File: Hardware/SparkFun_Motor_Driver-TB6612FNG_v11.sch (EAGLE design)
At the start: 14 parts, among them U1 TB6612FNG

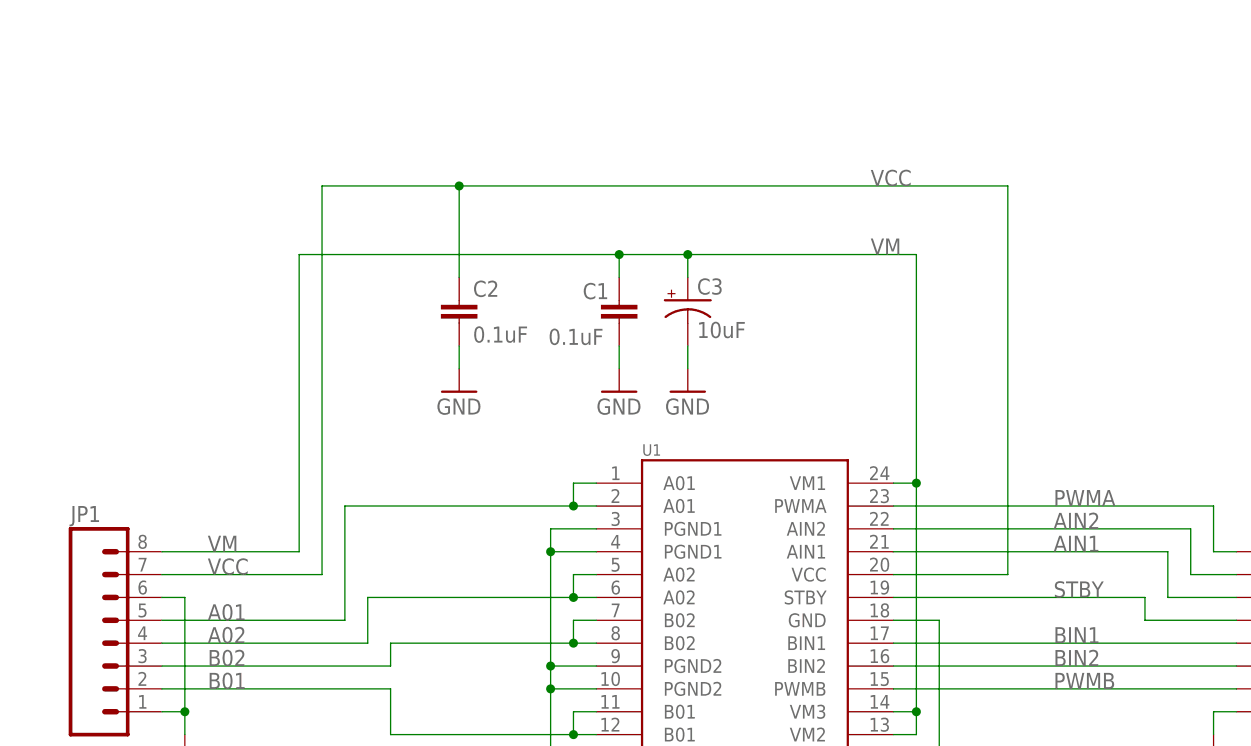
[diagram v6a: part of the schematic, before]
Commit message: schematic tweaks from double-check
-gave each VCC pin it's own net and VCC symbol
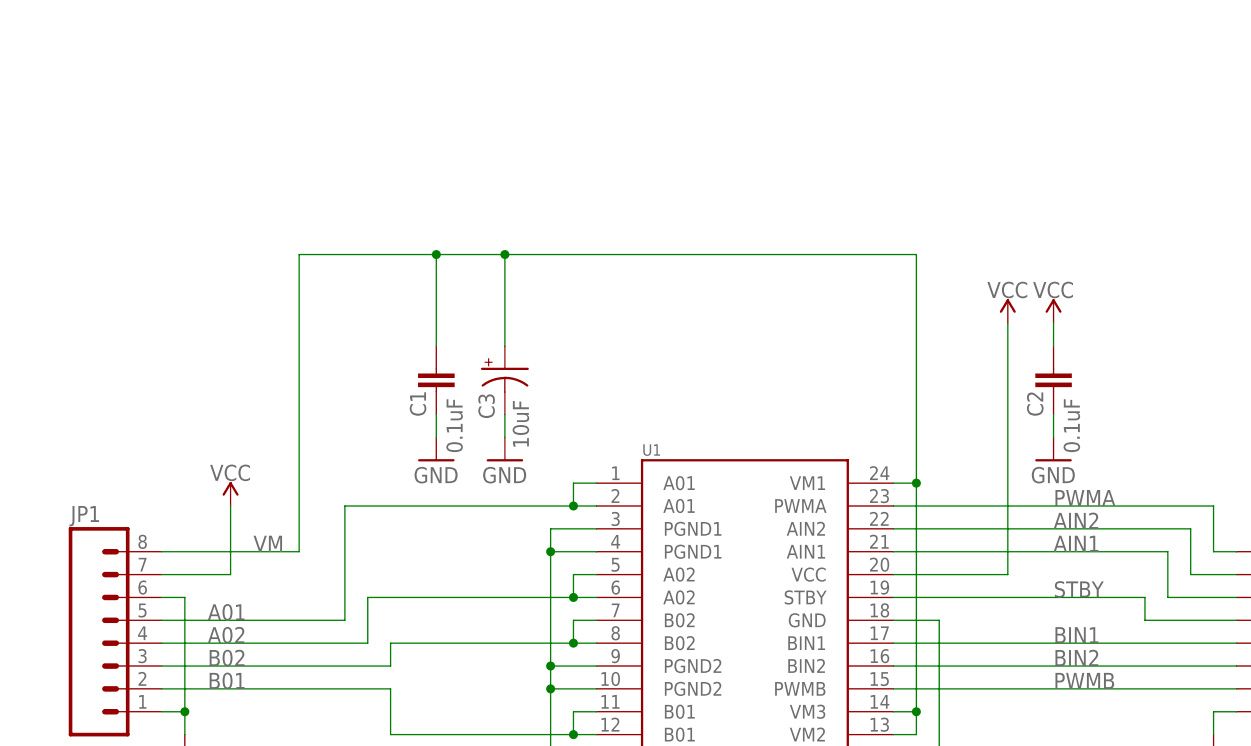
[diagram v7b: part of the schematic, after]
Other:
- moved on the sheet: C1, C2, C3
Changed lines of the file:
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@@
 <part name="FD3" library="SparkFun-Aesthetics" deviceset="FIDUCIAL" device="UFIDUCIAL"/>
 <part name="FD4" library="SparkFun-Aesthetics" deviceset="FIDUCIAL" device="UFIDUCIAL"/>
+<part name="SUPPLY1" library="SparkFun-PowerSymbols" deviceset="VCC" device=""/>
+<part name="SUPPLY2" library="SparkFun-PowerSymbols" deviceset="VCC" device=""/>
+<part name="SUPPLY3" library="SparkFun-PowerSymbols" deviceset="VCC" device=""/>
 </parts>
 <sheets>
@@
 <instances>
 <instance part="U1" gate="G$1" x="129.54" y="99.06"/>
-<instance part="C1" gate="G$1" x="114.3" y="129.54" smashed="yes">
-<attribute name="NAME" x="110.236" y="132.207" size="1.778" layer="95"/>
-<attribute name="VALUE" x="106.426" y="127.127" size="1.778" layer="96"/>
+<instance part="C1" gate="G$1" x="93.98" y="121.92" smashed="yes">
+<attribute name="NAME" x="92.837" y="119.126" size="1.778" layer="95" rot="R90"/>
+<attribute name="VALUE" x="96.901" y="115.062" size="1.778" layer="96" rot="R90"/>
 </instance>
-<instance part="C2" gate="G$1" x="96.52" y="129.54"/>
-<instance part="C3" gate="G$1" x="121.92" y="132.08" smashed="yes">
-<attribute name="NAME" x="122.936" y="132.715" size="1.778" layer="95"/>
-<attribute name="VALUE" x="122.936" y="127.889" size="1.778" layer="96"/>
+<instance part="C2" gate="G$1" x="162.56" y="121.92" smashed="yes">
+<attribute name="NAME" x="161.417" y="119.126" size="1.778" layer="95" font="vector" rot="R90"/>
+<attribute name="VALUE" x="165.481" y="115.062" size="1.778" layer="96" font="vector" rot="R90"/>
+</instance>
+<instance part="C3" gate="G$1" x="101.6" y="124.46" smashed="yes">
+<attribute name="NAME" x="100.457" y="118.872" size="1.778" layer="95" rot="R90"/>
+<attribute name="VALUE" x="104.267" y="115.57" size="1.778" layer="96" rot="R90"/>
 </instance>
 <instance part="JP1" gate="G$1" x="58.42" y="93.98"/>
 <instance part="JP2" gate="G$1" x="187.96" y="96.52" rot="R180"/>
 <instance part="GND1" gate="1" x="106.68" y="76.2"/>
-<instance part="GND2" gate="1" x="114.3" y="121.92"/>
-<instance part="GND3" gate="1" x="96.52" y="121.92"/>
-<instance part="GND4" gate="1" x="121.92" y="121.92"/>
+<instance part="GND2" gate="1" x="93.98" y="114.3"/>
+<instance part="GND3" gate="1" x="162.56" y="114.3"/>
+<instance part="GND4" gate="1" x="101.6" y="114.3"/>
 <instance part="GND5" gate="1" x="149.86" y="78.74"/>
 <instance part="GND6" gate="1" x="66.04" y="81.28"/>
@@
 <instance part="FD3" gate="G$1" x="236.22" y="38.1" rot="R90"/>
 <instance part="FD4" gate="G$1" x="231.14" y="38.1" rot="R90"/>
+<instance part="SUPPLY1" gate="G$1" x="157.48" y="129.54"/>
+<instance part="SUPPLY2" gate="G$1" x="71.12" y="109.22"/>
+<instance part="SUPPLY3" gate="G$1" x="162.56" y="129.54"/>
 </instances>
 <busses>
@@
 </segment>
 <segment>
-<wire x1="114.3" y1="124.46" x2="114.3" y2="127" width="0.1524" layer="91"/>
+<wire x1="93.98" y1="116.84" x2="93.98" y2="119.38" width="0.1524" layer="91"/>
 <pinref part="GND2" gate="1" pin="GND"/>
 <pinref part="C1" gate="G$1" pin="2"/>
 </segment>
 <segment>
-<wire x1="121.92" y1="127" x2="121.92" y2="124.46" width="0.1524" layer="91"/>
+<wire x1="101.6" y1="119.38" x2="101.6" y2="116.84" width="0.1524" layer="91"/>
 <pinref part="C3" gate="G$1" pin="-"/>
 <pinref part="GND4" gate="1" pin="GND"/>
 </segment>
 <segment>
-<wire x1="96.52" y1="124.46" x2="96.52" y2="127" width="0.1524" layer="91"/>
+<wire x1="162.56" y1="116.84" x2="162.56" y2="119.38" width="0.1524" layer="91"/>
 <pinref part="GND3" gate="1" pin="GND"/>
 <pinref part="C2" gate="G$1" pin="2"/>
@@
 <wire x1="144.78" y1="111.76" x2="147.32" y2="111.76" width="0.1524" layer="91"/>
 <wire x1="147.32" y1="111.76" x2="147.32" y2="137.16" width="0.1524" layer="91"/>
-<wire x1="147.32" y1="137.16" x2="121.92" y2="137.16" width="0.1524" layer="91"/>
-<wire x1="121.92" y1="137.16" x2="114.3" y2="137.16" width="0.1524" layer="91"/>
-<wire x1="114.3" y1="134.62" x2="114.3" y2="137.16" width="0.1524" layer="91"/>
-<wire x1="121.92" y1="134.62" x2="121.92" y2="137.16" width="0.1524" layer="91"/>
+<wire x1="147.32" y1="137.16" x2="101.6" y2="137.16" width="0.1524" layer="91"/>
+<wire x1="101.6" y1="137.16" x2="93.98" y2="137.16" width="0.1524" layer="91"/>
+<wire x1="93.98" y1="127" x2="93.98" y2="137.16" width="0.1524" layer="91"/>
+<wire x1="101.6" y1="127" x2="101.6" y2="137.16" width="0.1524" layer="91"/>
 <wire x1="63.5" y1="104.14" x2="78.74" y2="104.14" width="0.1524" layer="91"/>
-<wire x1="114.3" y1="137.16" x2="78.74" y2="137.16" width="0.1524" layer="91"/>
+<wire x1="93.98" y1="137.16" x2="78.74" y2="137.16" width="0.1524" layer="91"/>
 <wire x1="78.74" y1="137.16" x2="78.74" y2="104.14" width="0.1524" layer="91"/>
 <junction x="147.32" y="111.76"/>
 <junction x="147.32" y="86.36"/>
-<junction x="114.3" y="137.16"/>
-<junction x="121.92" y="137.16"/>
-<label x="142.24" y="137.16" size="1.778" layer="95"/>
-<label x="68.58" y="104.14" size="1.778" layer="95"/>
+<junction x="93.98" y="137.16"/>
+<junction x="101.6" y="137.16"/>
+<label x="73.66" y="104.14" size="1.778" layer="95"/>
 <pinref part="U1" gate="G$1" pin="VM2"/>
 <pinref part="U1" gate="G$1" pin="VM3"/>
@@
 <net name="VCC" class="0">
 <segment>
-<wire x1="63.5" y1="101.6" x2="81.28" y2="101.6" width="0.1524" layer="91"/>
-<wire x1="81.28" y1="101.6" x2="81.28" y2="144.78" width="0.1524" layer="91"/>
-<wire x1="81.28" y1="144.78" x2="96.52" y2="144.78" width="0.1524" layer="91"/>
-<wire x1="96.52" y1="144.78" x2="157.48" y2="144.78" width="0.1524" layer="91"/>
-<wire x1="157.48" y1="101.6" x2="157.48" y2="144.78" width="0.1524" layer="91"/>
+<pinref part="SUPPLY2" gate="G$1" pin="VCC"/>
+<wire x1="71.12" y1="101.6" x2="71.12" y2="109.22" width="0.1524" layer="91"/>
+<wire x1="63.5" y1="101.6" x2="71.12" y2="101.6" width="0.1524" layer="91"/>
+<pinref part="JP1" gate="G$1" pin="7"/>
+</segment>
+<segment>
+<pinref part="SUPPLY3" gate="G$1" pin="VCC"/>
+<wire x1="162.56" y1="127" x2="162.56" y2="129.54" width="0.1524" layer="91"/>
+<pinref part="C2" gate="G$1" pin="1"/>
+</segment>
+<segment>
+<wire x1="157.48" y1="101.6" x2="157.48" y2="129.54" width="0.1524" layer="91"/>
 <wire x1="144.78" y1="101.6" x2="157.48" y2="101.6" width="0.1524" layer="91"/>
-<wire x1="96.52" y1="134.62" x2="96.52" y2="144.78" width="0.1524" layer="91"/>
-<junction x="96.52" y="144.78"/>
-<label x="68.58" y="101.6" size="1.778" layer="95"/>
-<label x="142.24" y="144.78" size="1.778" layer="95"/>
-<pinref part="JP1" gate="G$1" pin="7"/>
 <pinref part="U1" gate="G$1" pin="VCC"/>
-<pinref part="C2" gate="G$1" pin="1"/>
-</segment>
-</net>
+<pinref part="SUPPLY1" gate="G$1" pin="VCC"/>
+</segment>
+</net>
